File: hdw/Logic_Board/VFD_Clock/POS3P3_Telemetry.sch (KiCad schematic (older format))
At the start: 15 parts

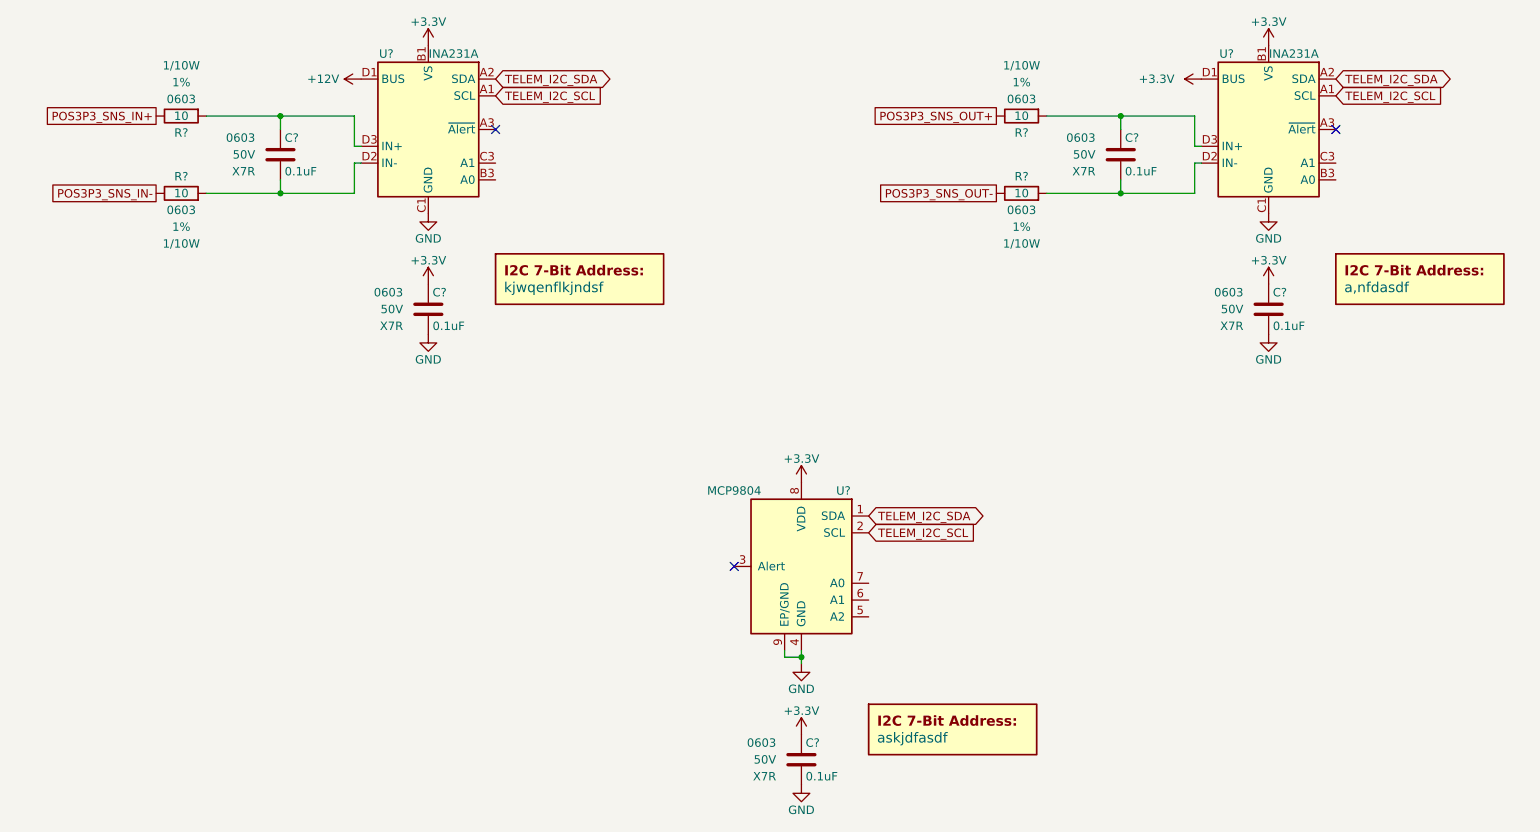
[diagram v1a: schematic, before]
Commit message: Lots of schematic additions
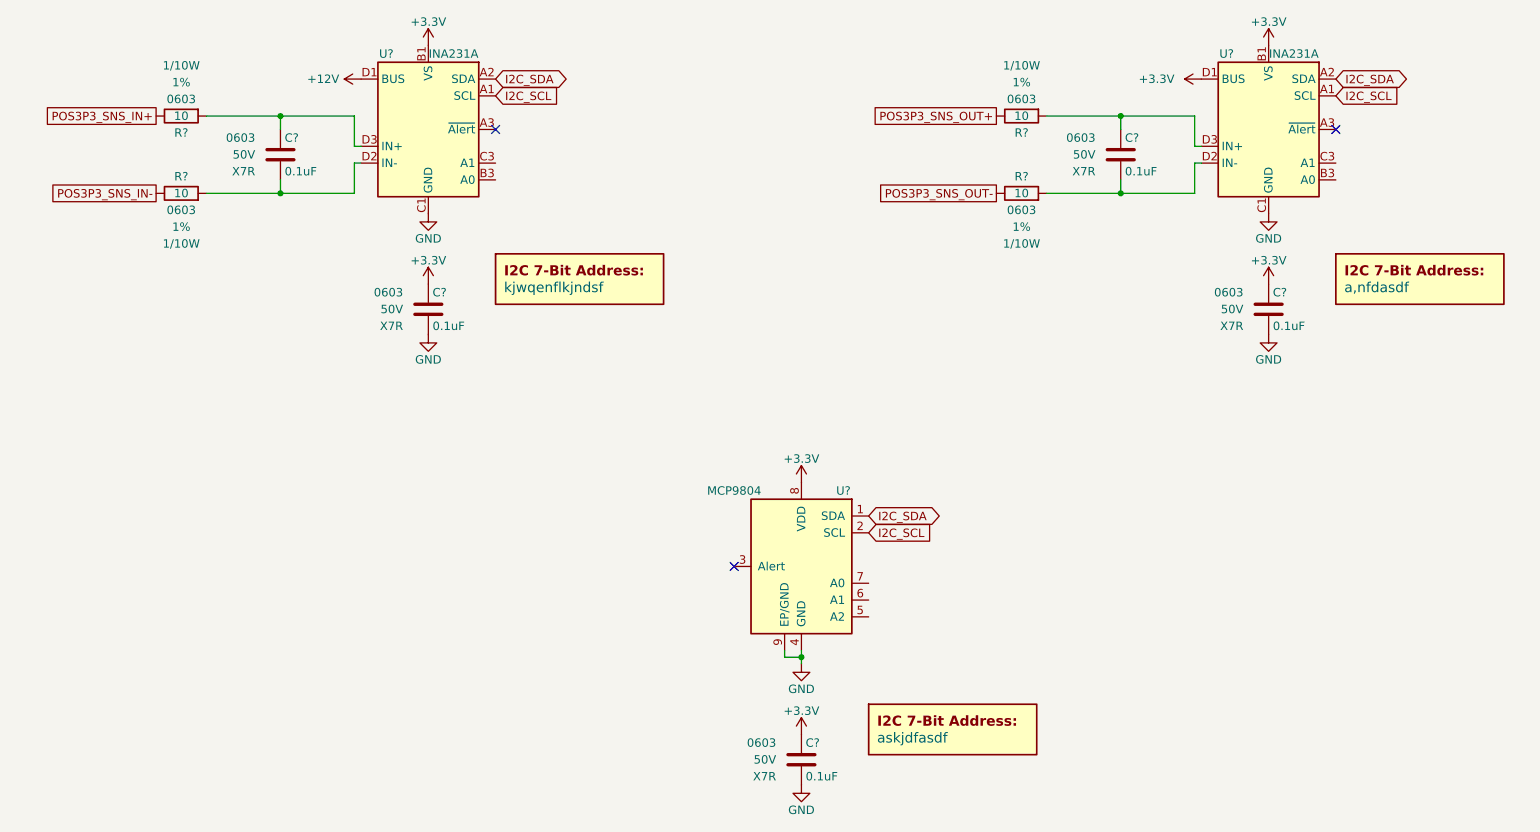
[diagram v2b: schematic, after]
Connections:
- net TELEM_I2C_SCL renamed I2C_SCL
- net TELEM_I2C_SDA renamed I2C_SDA
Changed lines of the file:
@@
 $Descr A 11000 8500
 encoding utf-8
-Sheet 21 26
+Sheet 20 28
 Title ""
 Date ""
@@
 $EndComp
 Text GLabel 3610 2040 2    50   Input ~ 0
-TELEM_I2C_SCL
+I2C_SCL
 $Comp
 L Custom_Library:C_Custom C?
@@
 $EndComp
 Text GLabel 3610 1940 2    50   BiDi ~ 0
-TELEM_I2C_SDA
+I2C_SDA
 NoConn ~ 3610 2240
 $Comp
@@
 $EndComp
 Text GLabel 5830 4640 2    50   Input ~ 0
-TELEM_I2C_SCL
+I2C_SCL
 Text GLabel 5830 4540 2    50   BiDi ~ 0
-TELEM_I2C_SDA
+I2C_SDA
 NoConn ~ 5030 4840
 $Comp
@@
 $EndComp
 Text GLabel 8610 2040 2    50   Input ~ 0
-TELEM_I2C_SCL
+I2C_SCL
 $Comp
 L Custom_Library:C_Custom C?
@@
 $EndComp
 Text GLabel 8610 1940 2    50   BiDi ~ 0
-TELEM_I2C_SDA
+I2C_SDA
 NoConn ~ 8610 2240
 $Comp

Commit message: Added backup RTC, IO connector, other stuff
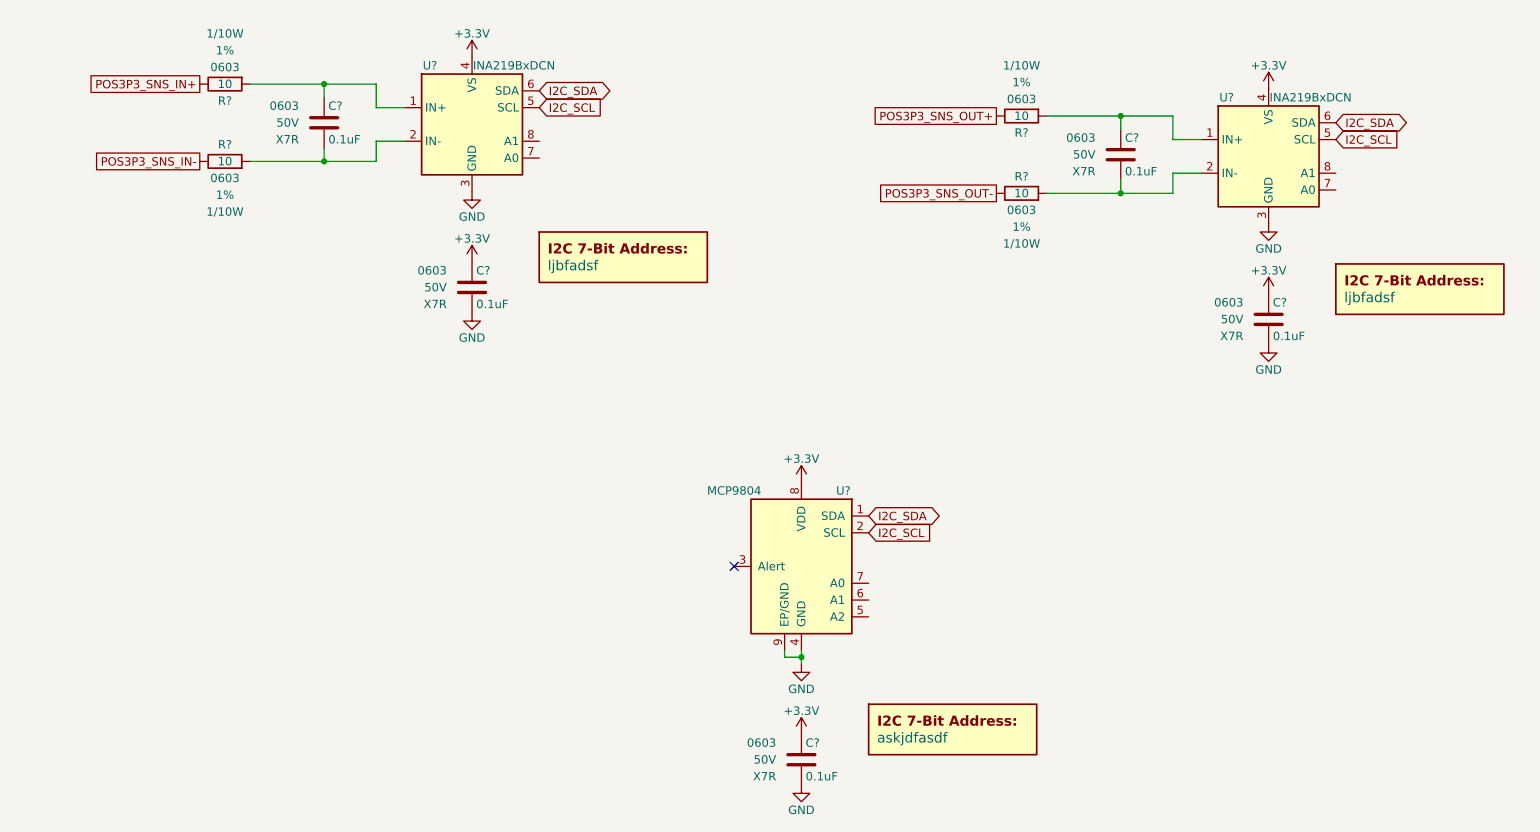
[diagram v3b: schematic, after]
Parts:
- removed C? (x4): 0.1uF, Capacitors_SMD:C_0603, symbol Custom_Library:C_Custom
- removed DOC?: a,nfdasdf, symbol Custom_Library:I2C_Address
- removed DOC?: kjwqenflkjndsf, symbol Custom_Library:I2C_Address
- removed R? (x4): 10, Resistors_SMD:R_0603, symbol Custom_Library:R_Custom
- removed U? (x2): INA231A, Custom Footprints Library:Texas_DSBGA-12_1.65x1.39mm_Layout3x4_P0.4mm, symbol Custom_Library:INA231A
- added C? (x4): 0.1uF, Capacitors_SMD:C_0603, symbol Custom_Library:C_Custom
- added DOC? (x2): ljbfadsf, symbol Custom_Library:I2C_Address
- added R? (x4): 10, Resistors_SMD:R_0603, symbol Custom_Library:R_Custom
- added U? (x2): INA219BxDCN, Package_TO_SOT_SMD:SOT-23-8, symbol Analog_ADC:INA219BxDCN
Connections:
- net +3V3: now also C?.1, C?.1, U?.4 (VS), U?.4 (VS)
- net GND: now also C?.2, C?.2, U?.3 (GND), U?.3 (GND)
- net I2C_SCL: now also U?.5 (SCL), U?.5 (SCL)
- net I2C_SDA: now also U?.6 (SDA), U?.6 (SDA)
- net POS3P3_SNS_IN+: now also R?.2
- net POS3P3_SNS_IN-: now also R?.2
- net POS3P3_SNS_OUT+: now also R?.2
- net POS3P3_SNS_OUT-: now also R?.2
- new net: C?.1, R?.1, U?.1 (IN+) (x2)
- new net: C?.2, R?.1, U?.2 (IN-) (x2)
- no-connect marks 3 -> 1

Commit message: Changed to configurable discrete gates, added VBAT stuff
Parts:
- removed C?: 0.1uF, Capacitors_SMD:C_0603, symbol Custom_Library:C_Custom
- removed DOC?: askjdfasdf, symbol Custom_Library:I2C_Address
- added C?: 0.1uF, Capacitors_SMD:C_0603, symbol Custom_Library:C_Custom
- added DOC?: askjdfasdf, symbol Custom_Library:I2C_Address
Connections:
- net +3V3: now also C?.1
- net GND: now also C?.2
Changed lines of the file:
@@
 $Comp
 L power:GND #PWR?
-U 1 1 5E0BDB8A
+U 1 1 5E2AA996
 P 5430 5420
-AR Path="/5B3E071A/5E0BDB8A" Ref="#PWR?"  Part="1"
-AR Path="/5E0652BA/5E0BDB8A" Ref="#PWR?"  Part="1"
-AR Path="/5E0A0E29/5E0BDB8A" Ref="#PWR?"  Part="1"
-AR Path="/5E0DC084/5E0BDB8A" Ref="#PWR?"  Part="1"
-AR Path="/5E0F263C/5E0BDB8A" Ref="#PWR?"  Part="1"
+AR Path="/5B3E071A/5E2AA996" Ref="#PWR?"  Part="1"
+AR Path="/5E0652BA/5E2AA996" Ref="#PWR?"  Part="1"
+AR Path="/5E0A0E29/5E2AA996" Ref="#PWR?"  Part="1"
+AR Path="/5E0DC084/5E2AA996" Ref="#PWR?"  Part="1"
+AR Path="/5E0F263C/5E2AA996" Ref="#PWR?"  Part="1"
 F 0 "#PWR?" H 5430 5170 50  0001 C CNN
 F 1 "GND" H 5430 5270 50  0000 C CNN
@@
 $Comp
 L power:+3.3V #PWR?
-U 1 1 5E0BDB95
+U 1 1 5E2AA998
 P 5430 4340
-AR Path="/5E0652BA/5E0BDB95" Ref="#PWR?"  Part="1"
-AR Path="/5E0A0E29/5E0BDB95" Ref="#PWR?"  Part="1"
-AR Path="/5E0DC084/5E0BDB95" Ref="#PWR?"  Part="1"
-AR Path="/5E0F263C/5E0BDB95" Ref="#PWR?"  Part="1"
+AR Path="/5E0652BA/5E2AA998" Ref="#PWR?"  Part="1"
+AR Path="/5E0A0E29/5E2AA998" Ref="#PWR?"  Part="1"
+AR Path="/5E0DC084/5E2AA998" Ref="#PWR?"  Part="1"
+AR Path="/5E0F263C/5E2AA998" Ref="#PWR?"  Part="1"
 F 0 "#PWR?" H 5430 4190 50  0001 C CNN
 F 1 "+3.3V" H 5430 4480 50  0000 C CNN
@@
 $Comp
 L Custom_Library:C_Custom C?
-U 1 1 5E0CB7AA
+U 1 1 5E2AA9A5
 P 5430 5990
-AR Path="/5B3E071A/5E0CB7AA" Ref="C?"  Part="1"
-AR Path="/5E0652BA/5E0CB7AA" Ref="C?"  Part="1"
-AR Path="/5E0A0E29/5E0CB7AA" Ref="C?"  Part="1"
-AR Path="/5E0DC084/5E0CB7AA" Ref="C?"  Part="1"
-AR Path="/5E0F263C/5E0CB7AA" Ref="C?"  Part="1"
+AR Path="/5B3E071A/5E2AA9A5" Ref="C?"  Part="1"
+AR Path="/5E0652BA/5E2AA9A5" Ref="C?"  Part="1"
+AR Path="/5E0A0E29/5E2AA9A5" Ref="C?"  Part="1"
+AR Path="/5E0DC084/5E2AA9A5" Ref="C?"  Part="1"
+AR Path="/5E0F263C/5E2AA9A5" Ref="C?"  Part="1"
 F 0 "C?" H 5455 6090 50  0000 L CNN
 F 1 "0.1uF" H 5455 5890 50  0000 L CNN
@@
 $Comp
 L power:+3.3V #PWR?
-U 1 1 5E0CB7B0
+U 1 1 5E2AA9A9
 P 5430 5840
-AR Path="/5E0652BA/5E0CB7B0" Ref="#PWR?"  Part="1"
-AR Path="/5E0A0E29/5E0CB7B0" Ref="#PWR?"  Part="1"
-AR Path="/5E0DC084/5E0CB7B0" Ref="#PWR?"  Part="1"
-AR Path="/5E0F263C/5E0CB7B0" Ref="#PWR?"  Part="1"
+AR Path="/5E0652BA/5E2AA9A9" Ref="#PWR?"  Part="1"
+AR Path="/5E0A0E29/5E2AA9A9" Ref="#PWR?"  Part="1"
+AR Path="/5E0DC084/5E2AA9A9" Ref="#PWR?"  Part="1"
+AR Path="/5E0F263C/5E2AA9A9" Ref="#PWR?"  Part="1"
 F 0 "#PWR?" H 5430 5690 50  0001 C CNN
 F 1 "+3.3V" H 5430 5980 50  0000 C CNN
@@
 $Comp
 L power:GND #PWR?
-U 1 1 5E0CB7B6
+U 1 1 5E2AA9AC
 P 5430 6140
-AR Path="/5E0652BA/5E0CB7B6" Ref="#PWR?"  Part="1"
-AR Path="/5E0A0E29/5E0CB7B6" Ref="#PWR?"  Part="1"
-AR Path="/5E0DC084/5E0CB7B6" Ref="#PWR?"  Part="1"
-AR Path="/5E0F263C/5E0CB7B6" Ref="#PWR?"  Part="1"
+AR Path="/5E0652BA/5E2AA9AC" Ref="#PWR?"  Part="1"
+AR Path="/5E0A0E29/5E2AA9AC" Ref="#PWR?"  Part="1"
+AR Path="/5E0DC084/5E2AA9AC" Ref="#PWR?"  Part="1"
+AR Path="/5E0F263C/5E2AA9AC" Ref="#PWR?"  Part="1"
 F 0 "#PWR?" H 5430 5890 50  0001 C CNN
 F 1 "GND" H 5430 5990 50  0000 C CNN
@@
 $Comp
 L Custom_Library:I2C_Address DOC?
-U 1 1 5E0CB7BC
+U 1 1 5E2AA9B2
 P 6330 5860
-AR Path="/5E0652BA/5E0CB7BC" Ref="DOC?"  Part="1"
-AR Path="/5E0A0E29/5E0CB7BC" Ref="DOC?"  Part="1"
-AR Path="/5E0DC084/5E0CB7BC" Ref="DOC?"  Part="1"
-AR Path="/5E0F263C/5E0CB7BC" Ref="DOC?"  Part="1"
+AR Path="/5E0652BA/5E2AA9B2" Ref="DOC?"  Part="1"
+AR Path="/5E0A0E29/5E2AA9B2" Ref="DOC?"  Part="1"
+AR Path="/5E0DC084/5E2AA9B2" Ref="DOC?"  Part="1"
+AR Path="/5E0F263C/5E2AA9B2" Ref="DOC?"  Part="1"
 F 0 "DOC?" H 6330 6110 60  0001 C CNN
 F 1 "askjdfasdf" H 5880 5860 60  0000 L CNN
